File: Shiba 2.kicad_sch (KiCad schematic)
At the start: 38 parts, among them J1 Conn_01x04_Pin, U1 STM32F072C8Tx, U3 AP62150Z6, U5 MIC5504-3.3YM5

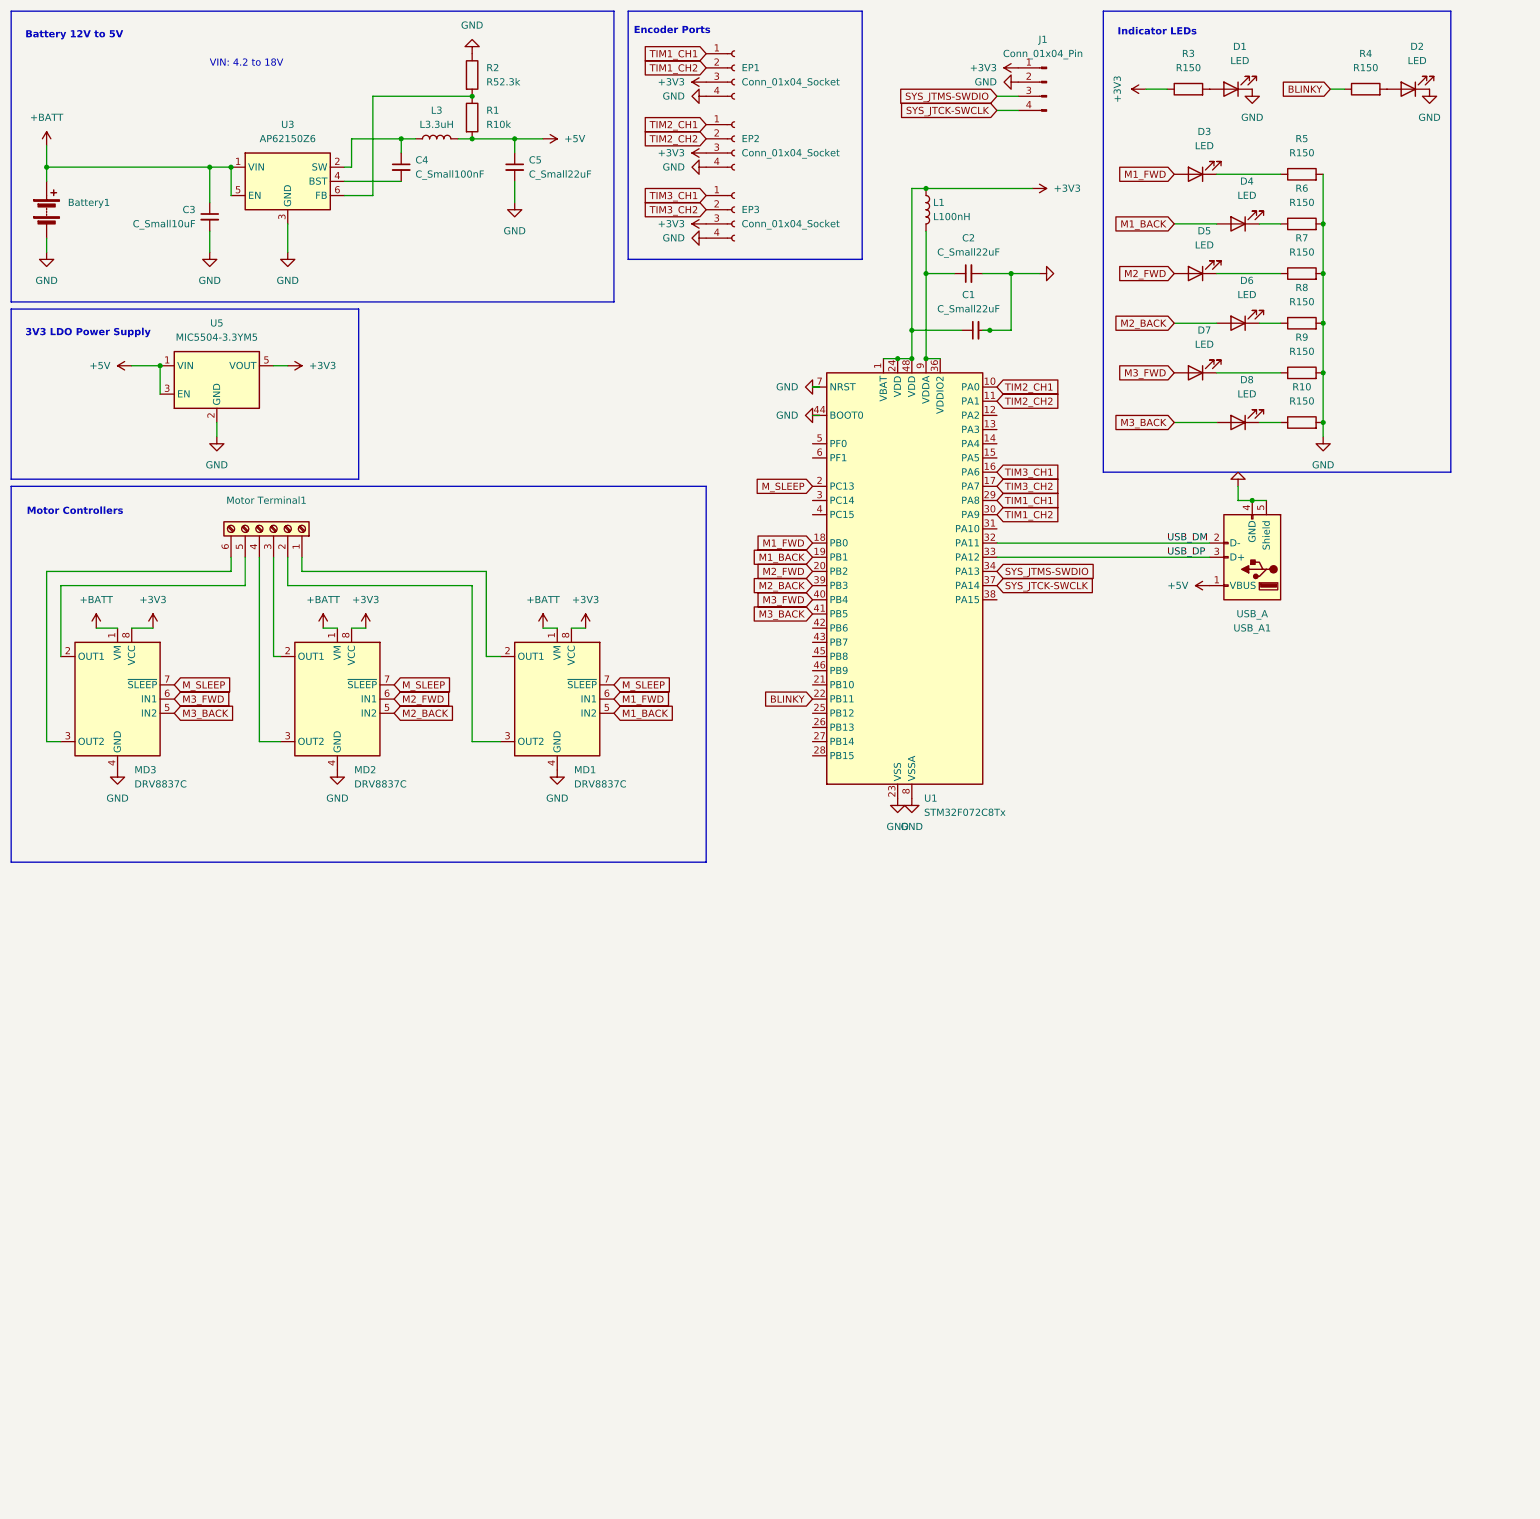
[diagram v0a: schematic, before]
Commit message: About ready to order but I realized I used underpowered motor drivers
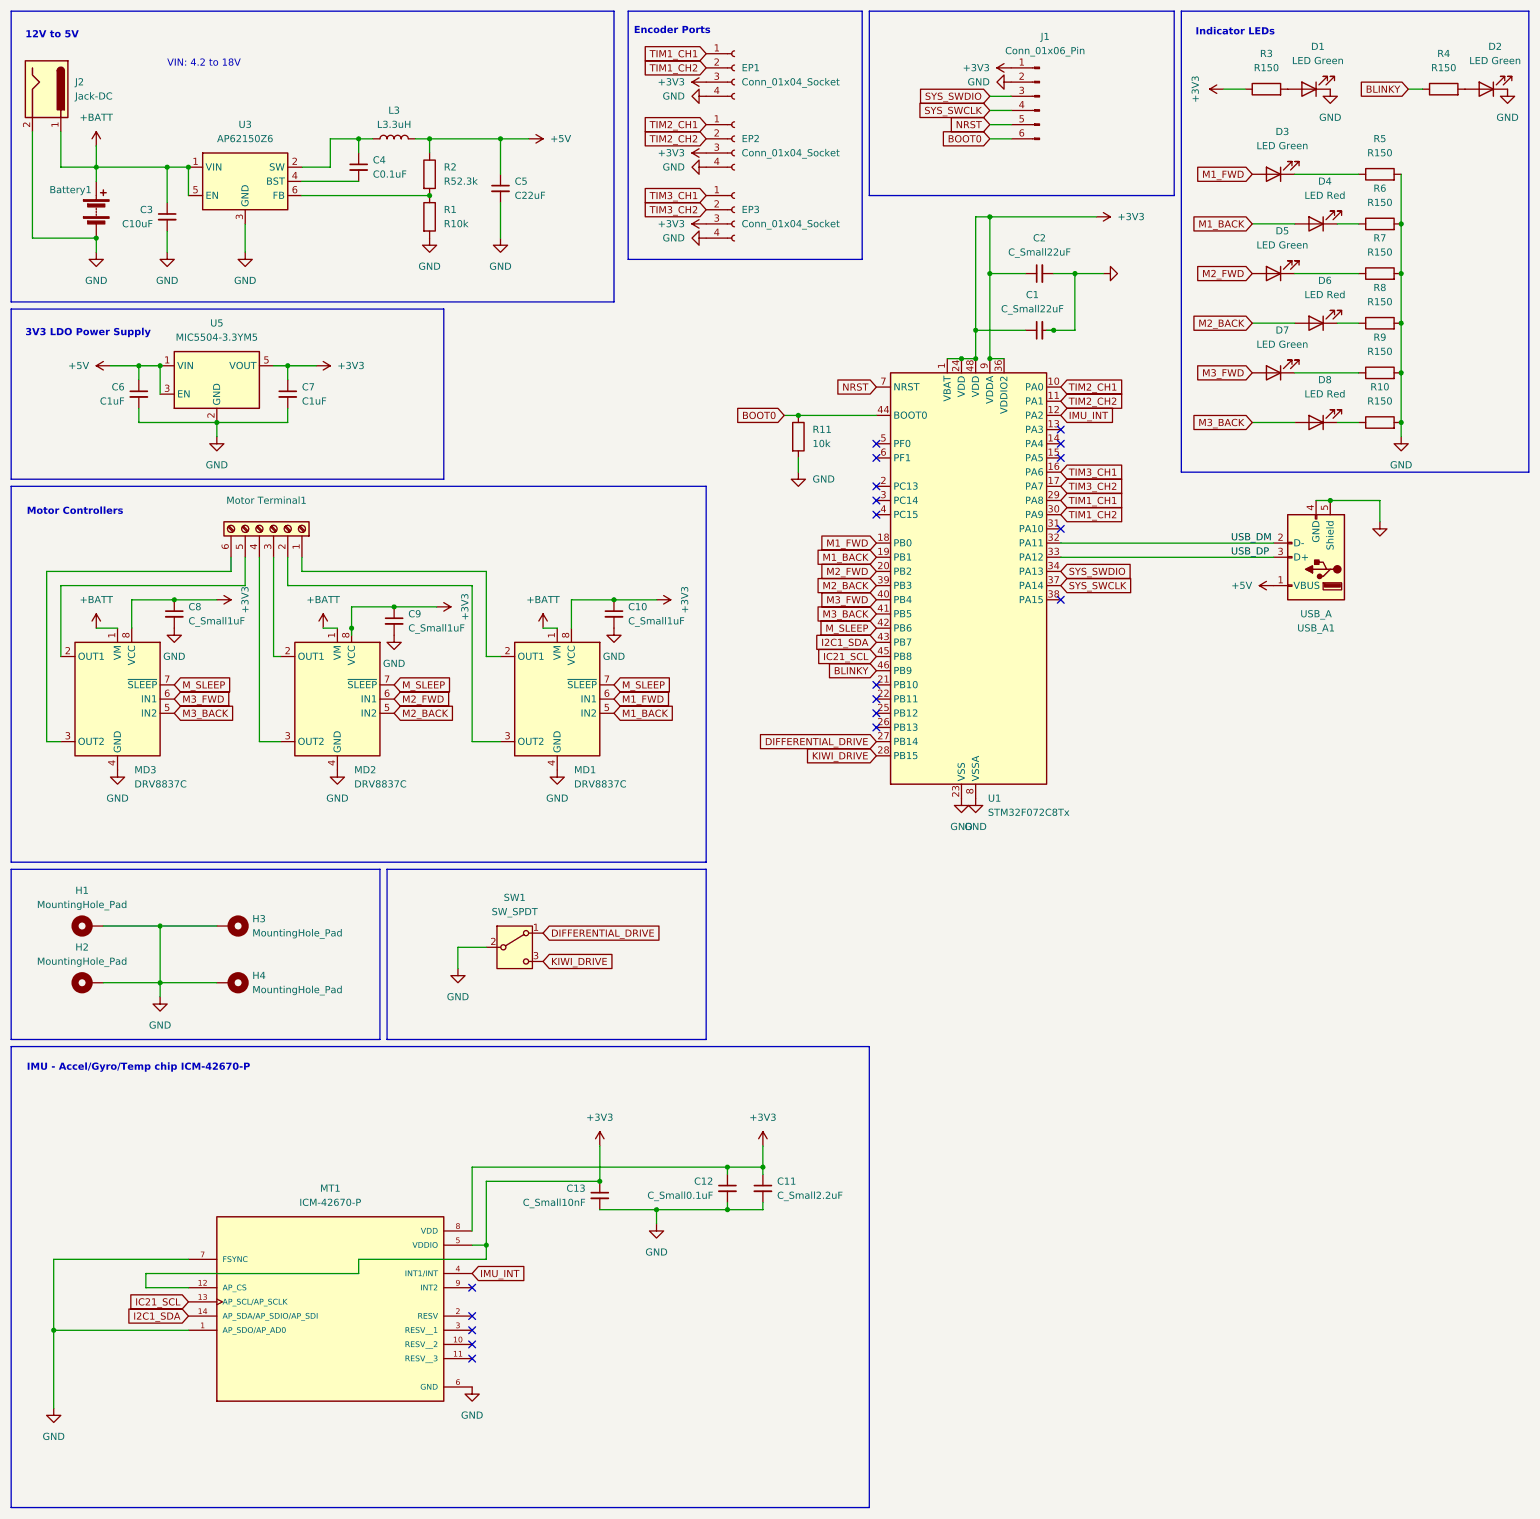
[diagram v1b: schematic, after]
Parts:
- removed J1: Conn_01x04_Pin, Connector_PinHeader_2.54mm:PinHeader_1x04_P2.54mm_Vertical, symbol Connector:Conn_01x04_Pin
- removed L1: L100nH, Inductor_SMD:L_1206_3216Metric, symbol Device:L
- added C10, C8, C9: C_Small1uF, Capacitor_SMD:C_1206_3216Metric, symbol Device:C_Small
- added C11: C_Small2.2uF, Capacitor_SMD:C_1206_3216Metric, symbol Device:C_Small
- added C12: C_Small0.1uF, Capacitor_SMD:C_1206_3216Metric, symbol Device:C_Small
- added C13: C_Small10nF, Capacitor_SMD:C_1206_3216Metric, symbol Device:C_Small
- added C6, C7: C1uF, Capacitor_SMD:C_1206_3216Metric, symbol Device:C_Small
- added H1, H2, H3, H4: MountingHole_Pad, MountingHole:MountingHole_2.2mm_M2_DIN965_Pad, symbol Mechanical:MountingHole_Pad
- added J1: Conn_01x06_Pin, Connector_PinHeader_2.54mm:PinHeader_1x06_P2.54mm_Vertical, symbol Connector:Conn_01x06_Pin
- added J2: Jack-DC, Connector_BarrelJack:BarrelJack_CUI_PJ-063AH_Horizontal, symbol Connector:Jack-DC
- added MT1: ICM-42670-P, Library:XDCR_ICM-42670-P, symbol ICM-42670-P:ICM-42670-P
- added R11: 10k, Resistor_SMD:R_1206_3216Metric, symbol Device:R
- added SW1: SW_SPDT, Button_Switch_THT:SW_E-Switch_EG1271_SPDT, symbol Switch:SW_SPDT
- Battery1: footprint TerminalBlock_4Ucon:TerminalBlock_4Ucon_1x02_P3.50mm_Horizontal -> Connector_AMASS:AMASS_XT60-F_1x02_P7.20mm_Vertical; DigiKey Part (none) -> PRT-10474
- C1, C2: DigiKey Part (none) -> GRM188R60J226MEA0J
- C3: value C_Small10uF -> C10uF; DigiKey Part (none) -> CL21A106KOQNNNE
- C4: value C_Small100nF -> C0.1uF; DigiKey Part (none) -> 1206B104K500BD
- C5: value C_Small22uF -> C22uF; DigiKey Part (none) -> GRM188R60J226MEA0J
- D1, D2, D3, D5, D7: value LED -> LED Green
- D4, D6, D8: value LED -> LED Red
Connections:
- net +3V3: now also C2.1, U1.36 (VDDIO2), U1.9 (VDDA), C10.1, C11.1, C12.1, C13.1, C7.1, C8.1, C9.1, J1.1 (Pin_1), MT1.12 (AP_CS), MT1.5 (VDDIO), MT1.8 (VDD)
- net +5V: now also R2.1, C6.1; no longer R1.2
- net +BATT: now also J2.1
- net BLINKY: now also U1.46 (PB9); no longer U1.22 (PB11)
- net GND: now also R1.2, C10.2, C11.2, C12.2, C13.2, C6.2, C7.2, C8.2, C9.2, H1.1, H2.1, H3.1, H4.1, J1.2 (Pin_2), J2.2, MT1.1 (AP_SDO/AP_AD0), MT1.6 (GND), MT1.7 (FSYNC), R11.2, SW1.2 (B); no longer R2.1, U1.44 (BOOT0), U1.7 (NRST)
- net M_SLEEP: now also U1.42 (PB6); no longer U1.2 (PC13)
- net IMU_INT: now reaches U1.12 (PA2)
- net IMU_INT: now also MT1.4 (INT1/INT)
- net DIFFERENTIAL_DRIVE: now reaches U1.27 (PB14)
- net DIFFERENTIAL_DRIVE: now also SW1.1 (A)
- net KIWI_DRIVE: now reaches U1.28 (PB15)
- net KIWI_DRIVE: now also SW1.3 (C)
- net I2C1_SDA: now reaches U1.43 (PB7)
- net I2C1_SDA: now also MT1.14 (AP_SDA/AP_SDIO/AP_SDI)
- net IC21_SCL: now reaches U1.45 (PB8)
- net IC21_SCL: now also MT1.13 (AP_SCL/AP_SCLK)
- net SYS_JTCK-SWCLK renamed SYS_SWCLK
- net SYS_SWCLK: now also J1.4 (Pin_4)
- net SYS_JTMS-SWDIO renamed SYS_SWDIO
- net SYS_SWDIO: now also J1.3 (Pin_3)
- new net BOOT0: J1.6 (Pin_6), R11.1, U1.44 (BOOT0)
- new net NRST: J1.5 (Pin_5), U1.7 (NRST)
- no-connect marks 0 -> 19
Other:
- note added: "12V to 5V"
- note added: "IMU - Accel/Gyro/Temp chip ICM-42670-P"
- note removed: "Battery 12V to 5V"
- moved on the sheet: Battery1, C1, C2, C3, C4, C5, D1, D2, D3, D4, D5, D6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

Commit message: REV 1 ORDERED WOOOOO
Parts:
- removed C9: C_Small1uF, Capacitor_SMD:C_1206_3216Metric, symbol Device:C_Small
- removed MD1, MD2, MD3: DRV8837C, Package_SON:WSON-8-1EP_2x2mm_P0.5mm_EP0.9x1.6mm, symbol Driver_Motor:DRV8837C
- added C15: C1uF, Capacitor_SMD:C_1206_3216Metric, symbol Device:C_Small
- added J3: Conn_01x010_Pin, Connector_PinSocket_2.54mm:PinSocket_1x10_P2.54mm_Vertical, symbol Connector:Conn_01x10_Pin
- added MD1, MD2, MD3: ZXBM5210-S, Package_SO:SOIC-8_3.9x4.9mm_P1.27mm, symbol Driver_Motor:ZXBM5210-S
- added R12, R13: R10k, Resistor_SMD:R_1206_3216Metric, symbol Device:R
- C10, C8: value C_Small1uF -> C1uF; DigiKey Part (none) -> CL21A106KOQNNNE
- renumbered U3 to U1, U5 to U2, U1 to U3
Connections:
- net +3V3: now also C15.1, J3.10 (Pin_10), MD1.3 (VDD), MD1.6 (VREF), MD2.3 (VDD), MD2.6 (VREF), MD3.3 (VDD), MD3.6 (VREF), R12.2, R13.2
- net +BATT: now also MD1.2 (VM), MD2.2 (VM), MD3.2 (VM)
- net GND: now also C15.2, J3.9 (Pin_9), MD1.8 (GND), MD2.8 (GND), MD3.8 (GND)
- net I2C1_SDA: now also R12.1
- net IC21_SCL: now also R13.1
- net M1_FWD: now also MD3.5 (REV)
- net M2_FWD: now also MD2.5 (REV)
- net M3_FWD: now also MD1.5 (REV)
- net GPIO_5: now reaches U3.13 (PA3)
- net GPIO_5: now also J3.3 (Pin_3)
- net GPIO_6: now reaches U3.14 (PA4)
- net GPIO_6: now also J3.2 (Pin_2)
- net GPIO_7: now reaches U3.15 (PA5)
- net GPIO_7: now also J3.1 (Pin_1)
- net GPIO_0: now reaches U3.2 (PC13)
- net GPIO_0: now also J3.8 (Pin_8)
- net GPIO_1: now reaches U3.3 (PC14)
- net GPIO_1: now also J3.7 (Pin_7)
- net GPIO_2: now reaches U3.4 (PC15)
- net GPIO_2: now also J3.6 (Pin_6)
- net GPIO_3: now reaches U3.5 (PF0)
- net GPIO_3: now also J3.5 (Pin_5)
- net GPIO_4: now reaches U3.6 (PF1)
- net GPIO_4: now also J3.4 (Pin_4)
- net at Motor Terminal1.1 (Pin_1): now also MD3.7 (OUT2)
- net at Motor Terminal1.2 (Pin_2): now also MD3.1 (OUT1)
- net at Motor Terminal1.5 (Pin_5): now also MD1.7 (OUT2)
- net at Motor Terminal1.6 (Pin_6): now also MD1.1 (OUT1)
- net at Motor Terminal1.3 (Pin_3): now also MD2.7 (OUT2)
- net at Motor Terminal1.4 (Pin_4): now also MD2.1 (OUT1)
- net M1_BACK renamed M1_REV
- net M1_REV: now also MD3.4 (FWD)
- net M2_BACK renamed M2_REV
- net M2_REV: now also MD2.4 (FWD)
- net M3_BACK renamed M3_REV
- net M3_REV: now also MD1.4 (FWD)
- net M_SLEEP: no longer names the net of U3.42 (PB6)
- no-connect marks 19 -> 11
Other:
- note added: "VREF is wired to VDD to enable PWM control"
- moved on the sheet: Motor Terminal1, R11

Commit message: going to prepare BOM for Rev 1 order
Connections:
- net DIFFERENTIAL_DRIVE: no longer names the net of SW1.1 (A)
- net DIFFERENTIAL_DRIVE: no longer U3.27 (PB14)
- no-connect marks 11 -> 14

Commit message: Rev 1 BOM ordered let's goooooo!
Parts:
- Battery1: DigiKey Part PRT-10474 -> (none)
- C1, C2: value C_Small22uF -> C1uF; footprint Capacitor_SMD:C_1206_3216Metric -> Capacitor_SMD:C_1206_3216Metric_Pad1.33x1.80mm_HandSolder; DigiKey (none) -> CL31B105KBHNNNE; DigiKey Part GRM188R60J226MEA0J -> (none)
- C10, C15, C6, C7, C8: footprint Capacitor_SMD:C_1206_3216Metric -> Capacitor_SMD:C_1206_3216Metric_Pad1.33x1.80mm_HandSolder; DigiKey (none) -> CL31B105KBHNNNE; DigiKey Part CL21A106KOQNNNE -> (none)
- C11: value C_Small2.2uF -> C2.2uF; footprint Capacitor_SMD:C_1206_3216Metric -> Capacitor_SMD:C_1206_3216Metric_Pad1.33x1.80mm_HandSolder; DigiKey (none) -> CL31B225KBHNFNE
- C12: value C_Small0.1uF -> C0.1uF; footprint Capacitor_SMD:C_1206_3216Metric -> Capacitor_SMD:C_1206_3216Metric_Pad1.33x1.80mm_HandSolder; DigiKey (none) -> C1206C104K5RAC7800
- C13: value C_Small10nF -> C0.01uF; footprint Capacitor_SMD:C_1206_3216Metric -> Capacitor_SMD:C_1206_3216Metric_Pad1.33x1.80mm_HandSolder; DigiKey (none) -> C1206C103K5RAC7025
- C3: footprint Capacitor_SMD:C_1206_3216Metric -> Capacitor_SMD:C_1206_3216Metric_Pad1.33x1.80mm_HandSolder; DigiKey (none) -> CL31B106KOHNNWE; DigiKey Part CL21A106KOQNNNE -> (none)
- C4: footprint Capacitor_SMD:C_1206_3216Metric -> Capacitor_SMD:C_1206_3216Metric_Pad1.33x1.80mm_HandSolder; DigiKey (none) -> C1206C104K5RAC7800; DigiKey Part 1206B104K500BD -> (none)
- C5: footprint Capacitor_SMD:C_1206_3216Metric -> Capacitor_SMD:C_1206_3216Metric_Pad1.33x1.80mm_HandSolder; DigiKey (none) -> CL31A226MOCLNNC; DigiKey Part GRM188R60J226MEA0J -> (none)
- D1, D2, D3, D5, D7: footprint LED_SMD:LED_1206_3216Metric -> LED_SMD:LED_1206_3216Metric_Pad1.42x1.75mm_HandSolder; DigiKey (none) -> 150120VS75000
- D4, D6, D8: footprint LED_SMD:LED_1206_3216Metric -> LED_SMD:LED_1206_3216Metric_Pad1.42x1.75mm_HandSolder; DigiKey (none) -> 150120RS75000
- EP1, EP2, EP3, J3: DigiKey (none) -> 2.54mm Pin Socket
- H1, H2, H3, H4: now not fitted
- J1: DigiKey (none) -> 2.54mm Pin Header
- J2: DigiKey (none) -> PJ-037A
- L3: DigiKey (none) -> LQM31PN3R3M00L
- MD1, MD2, MD3: DigiKey (none) -> ZXBM5210-S-1
- MT1: DigiKey (none) -> ICM-42670-P
- Motor Terminal1: DigiKey (none) -> OQ0612510000G
- R1, R12, R13: footprint Resistor_SMD:R_1206_3216Metric -> Resistor_SMD:R_1206_3216Metric_Pad1.30x1.75mm_HandSolder; DigiKey (none) -> RC1206FR-0710KL
- R10, R3, R4, R5, R6, R7, R8, R9: footprint Resistor_SMD:R_1206_3216Metric -> Resistor_SMD:R_1206_3216Metric_Pad1.30x1.75mm_HandSolder; DigiKey (none) -> RG1005P-151-B-T5
- R11: value 10k -> R10k; footprint Resistor_SMD:R_1206_3216Metric -> Resistor_SMD:R_1206_3216Metric_Pad1.30x1.75mm_HandSolder; DigiKey (none) -> RC1206FR-0710KL
- R2: footprint Resistor_SMD:R_1206_3216Metric -> Resistor_SMD:R_1206_3216Metric_Pad1.30x1.75mm_HandSolder; DigiKey (none) -> CRCW120652K3FKEA
- SW1: DigiKey (none) -> EG1271A
- U1: DigiKey (none) -> AP62150Z6-7
- U2: DigiKey (none) -> MIC5504-3.3YM5
- U3: DigiKey (none) -> STM32F072C8T6TR
- USB_A1: DigiKey (none) -> USB-A1HSB6

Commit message: Rev 1 BOM order save
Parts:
- Battery1: DigiKey (none) -> PRT-10474
- R10, R3, R4, R5, R6, R7, R8, R9: DigiKey RG1005P-151-B-T5 -> P150BCCT-ND
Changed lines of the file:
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@@
 			)
 		)
-		(property "DigiKey" "RG1005P-151-B-T5"
+		(property "DigiKey" "P150BCCT-ND"
 			(at 257.81 59.69 0)
 			(effects
@@
 			)
 		)
-		(property "DigiKey" "RG1005P-151-B-T5"
+		(property "DigiKey" "P150BCCT-ND"
 			(at 257.81 86.36 0)
 			(effects
@@
 			)
 		)
-		(property "DigiKey" "RG1005P-151-B-T5"
+		(property "DigiKey" "P150BCCT-ND"
 			(at 269.24 26.67 0)
 			(effects
@@
 			)
 		)
-		(property "DigiKey" "RG1005P-151-B-T5"
+		(property "DigiKey" "P150BCCT-ND"
 			(at 237.49 26.67 0)
 			(effects
@@
 			)
 		)
-		(property "DigiKey" "RG1005P-151-B-T5"
+		(property "DigiKey" "P150BCCT-ND"
 			(at 257.81 68.58 0)
 			(effects
@@
 			)
 		)
-		(property "DigiKey" "RG1005P-151-B-T5"
+		(property "DigiKey" "P150BCCT-ND"
 			(at 257.81 50.8 0)
 			(effects
@@
 			)
 		)
-		(property "DigiKey" "RG1005P-151-B-T5"
+		(property "DigiKey" "P150BCCT-ND"
 			(at 257.81 41.91 0)
 			(effects
@@
 			)
 		)
+		(property "DigiKey" "PRT-10474"
+			(at 27.94 48.26 0)
+			(effects
+				(font
+					(size 1.27 1.27)
+				)
+				(hide yes)
+			)
+		)
 		(pin "1"
 		)
@@
 			)
 		)
-		(property "DigiKey" "RG1005P-151-B-T5"
+		(property "DigiKey" "P150BCCT-ND"
 			(at 257.81 77.47 0)
 			(effects

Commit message: Rev 2 maybe?
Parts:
- removed J3: Conn_01x010_Pin, Connector_PinSocket_2.54mm:PinSocket_1x10_P2.54mm_Vertical, symbol Connector:Conn_01x10_Pin
- removed U3: STM32F072C8Tx, Package_QFP:LQFP-48_7x7mm_P0.5mm, symbol MCU_ST_STM32F0:STM32F072C8Tx
- added C14, C9: C2.2uF, Capacitor_SMD:C_1206_3216Metric_Pad1.33x1.80mm_HandSolder, symbol Device:C_Small
- added C16: C1uF, Capacitor_SMD:C_1206_3216Metric_Pad1.33x1.80mm_HandSolder, symbol Device:C_Small
- added J3: GPIO, Connector_PinSocket_2.54mm:PinSocket_1x08_P2.54mm_Vertical, symbol Connector:Conn_01x08_Pin
- added J4: Conn_01x02_Pin, Connector_PinHeader_2.54mm:PinHeader_1x02_P2.54mm_Vertical, symbol Connector:Conn_01x02_Pin
- added J5, J6, J7, J8: Conn_01x03_Pin, Connector_PinSocket_2.54mm:PinSocket_1x03_P2.54mm_Vertical, symbol Connector:Conn_01x03_Pin
- added U4: STM32H503CBTx, Package_QFP:LQFP-48_7x7mm_P0.5mm, symbol MCU_ST_STM32H5:STM32H503CBTx
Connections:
- net +3V3: now also C16.2, J3.8 (Pin_8), U4.1 (VBAT), U4.24 (VDD), U4.36 (VDD), U4.48 (VDD), U4.9 (VDDA)
- net +5V: now also J5.2 (Pin_2), J6.2 (Pin_2), J7.2 (Pin_2), J8.2 (Pin_2)
- net BLINKY: now also U4.16 (PA6)
- net BOOT0: now also U4.44 (BOOT0)
- net GND: now also C14.2, C16.1, C9.2, J3.7 (Pin_7), J5.1 (Pin_1), J6.1 (Pin_1), J7.1 (Pin_1), J8.1 (Pin_1), U4.23 (VSS), U4.35 (VSS), U4.47 (VSS), U4.8 (VSSA)
- net GPIO_0: now also J3.6 (Pin_6), U4.13 (PA3)
- net GPIO_1: now also J3.5 (Pin_5), U4.6 (PH1)
- net GPIO_2: now also J3.4 (Pin_4), U4.5 (PH0)
- net GPIO_3: now also J3.3 (Pin_3), U4.4 (PC15)
- net GPIO_4: now also J3.2 (Pin_2), U4.3 (PC14)
- net GPIO_5: now also J3.1 (Pin_1), U4.2 (PC13)
- net I2C1_SDA: now also U4.21 (PB10)
- net KIWI_DRIVE: now also U4.14 (PA4)
- net M1_FWD: now also U4.45 (PB8)
- net M1_REV: now also U4.43 (PB7)
- net M2_FWD: now also U4.41 (PB5)
- net M2_REV: now also U4.40 (PB4(NJTRST))
- net M3_FWD: now also U4.27 (PB14)
- net M3_REV: now also U4.28 (PB15)
- net NRST: now also U4.7 (NRST)
- net SYS_SWCLK: now also U4.37 (PA14(JTCK)
- net SYS_SWDIO: now also U4.34 (PA13(JTMS)
- net TIM1_CH1: now also U4.19 (PB1)
- net TIM1_CH2: now also U4.30 (PA9)
- net TIM2_CH1: now also U4.15 (PA5)
- net TIM2_CH2: now also U4.39 (PB3(JTDO)
- net TIM3_CH1: now also U4.10 (PA0)
- net TIM3_CH2: now also U4.17 (PA7)
- net USB_DM: now also U4.32 (PA11)
- net USB_DP: now also U4.33 (PA12)
- net IC21_SCL renamed I2C1_SCL
- net I2C1_SCL: now also U4.42 (PB6)
- new net: C14.1, U4.22 (VCAP)
- new net: C9.1, U4.46 (VCAP)
- new net SERVO_0: J5.3 (Pin_3), U4.18 (PB0)
- new net SERVO_1: J6.3 (Pin_3), U4.20 (PB2)
- new net SERVO_2: J7.3 (Pin_3), U4.25 (PB12)
- new net SERVO_3: J8.3 (Pin_3), U4.26 (PB13)
- new net USART1_RX: J4.1 (Pin_1), U4.11 (PA1)
- new net USART1_TX: J4.2 (Pin_2), U4.12 (PA2)
- no-connect marks 14 -> 6
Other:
- moved on the sheet: D1, D2, D3, D4, D5, D6, D7, D8, R10, R3, R4, R5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

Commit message: more rev2 revisions
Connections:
- net USB_DM renamed USB_D-
- net USB_DP renamed USB_D+
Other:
- moved on the sheet: C14, C9
